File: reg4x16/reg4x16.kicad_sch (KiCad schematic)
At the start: 19 parts, among them J1 Conn_01x04, J2 Conn_01x01, U1 74LS670, U2 74LS670, U3 74LS670, U4 74LS670, U5 74AHC1G32, U6 74AHC1G32

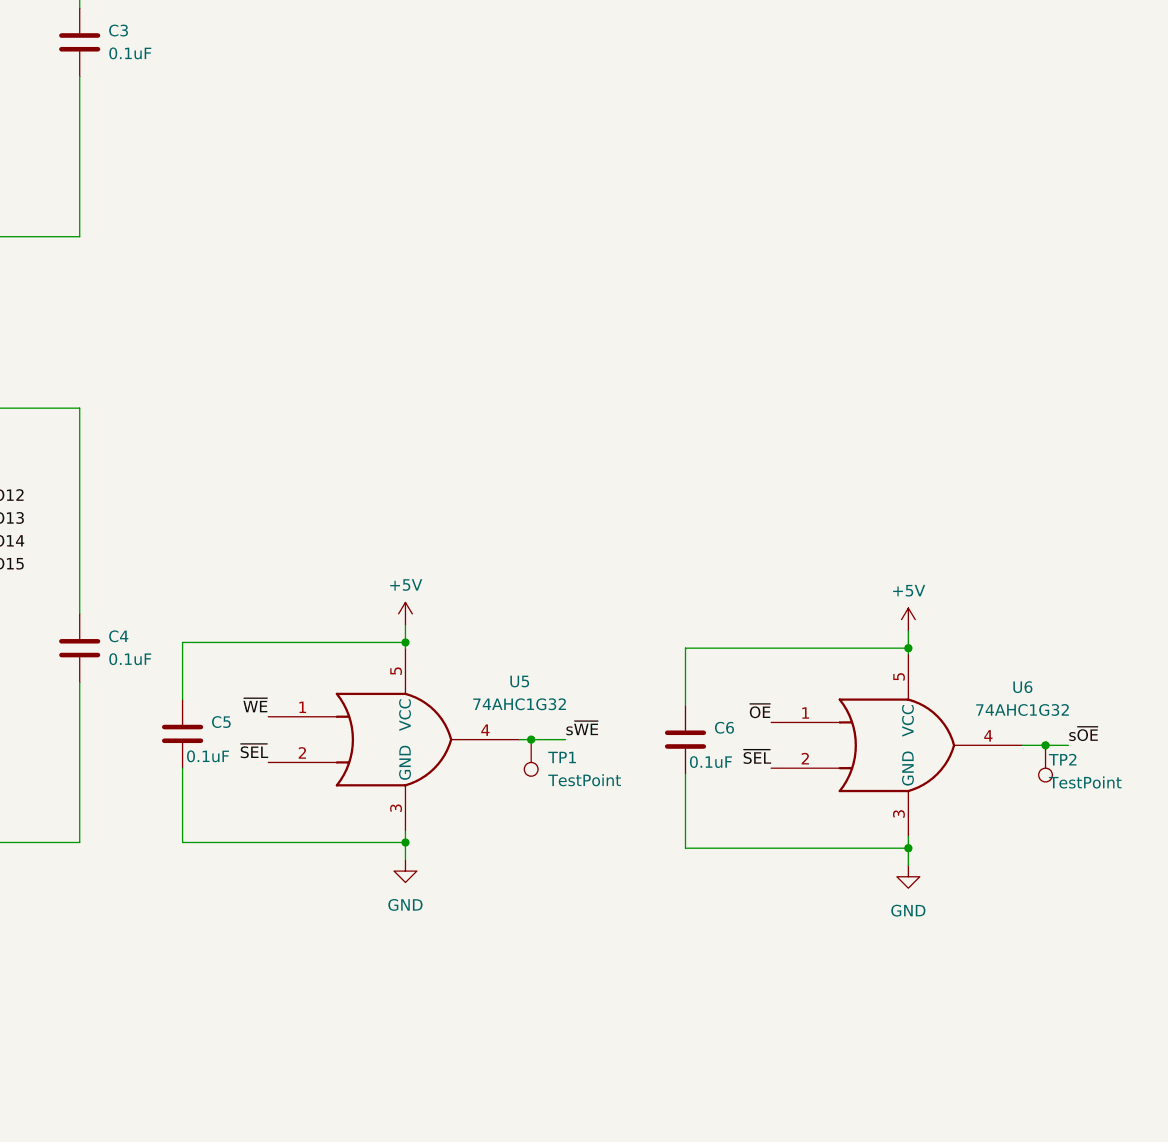
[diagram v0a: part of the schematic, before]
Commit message: Refactored files, finalized reg4x16, and used lowercase v
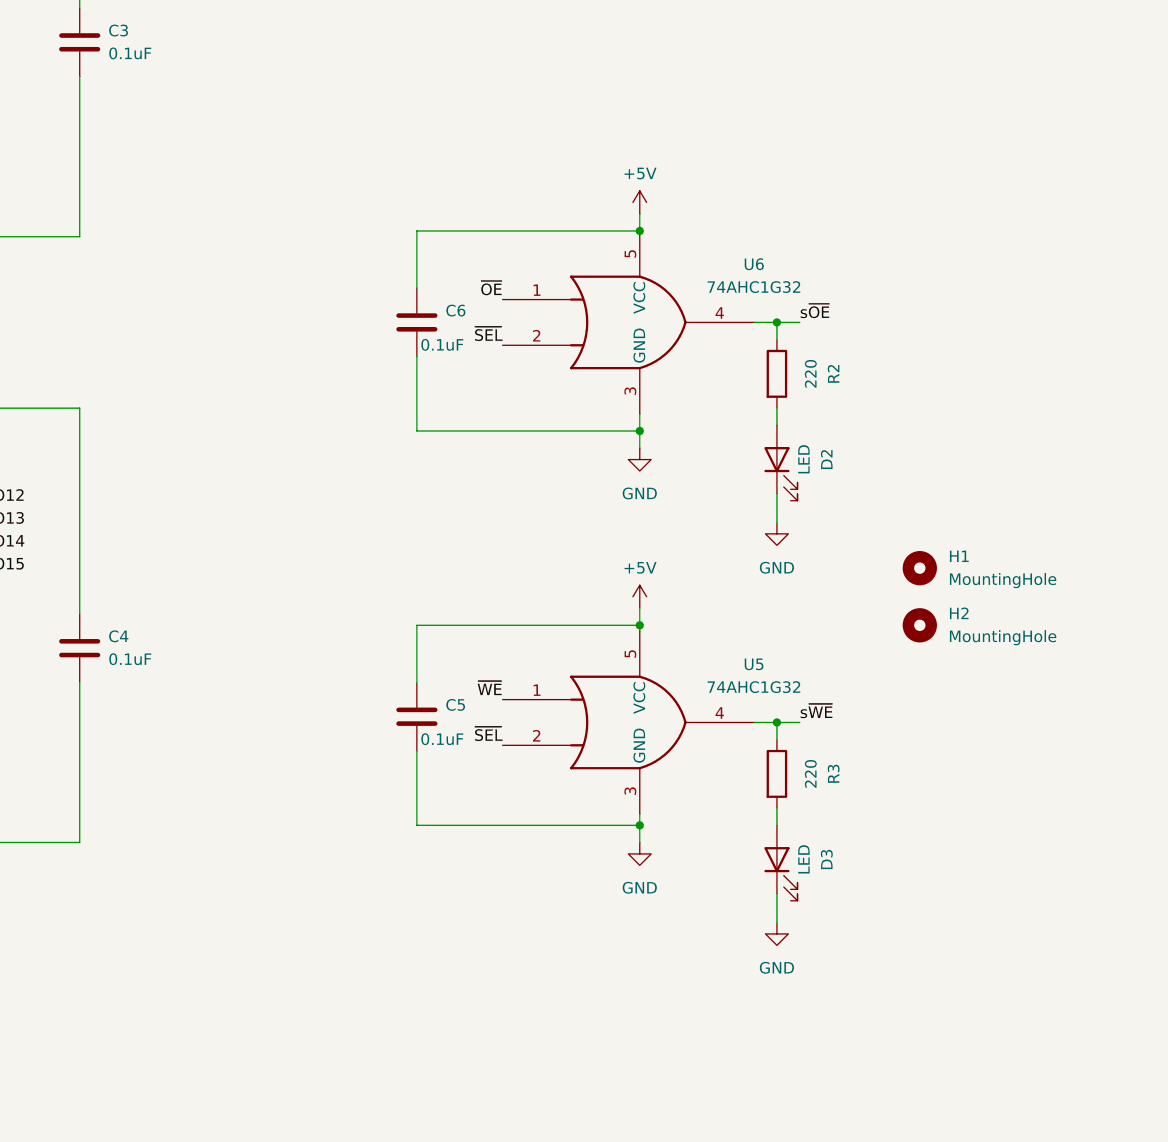
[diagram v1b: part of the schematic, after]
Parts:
- removed TP1, TP2: TestPoint, TestPoint:TestPoint_Pad_D2.0mm, symbol Connector:TestPoint
- added D2, D3: LED, LED_SMD:LED_0603_1608Metric, symbol Device:LED
- added H1, H2: MountingHole, MountingHole:MountingHole_2.2mm_M2, symbol Mechanical:MountingHole
- added R2, R3: 220, Resistor_SMD:R_0603_1608Metric, symbol Device:R
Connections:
- net GND: now also D2.1 (K), D3.1 (K)
- net s~{OE}: now also R2.1
- net s~{WE}: now also R3.1
- new net: D3.2 (A), R3.2
- new net: D2.2 (A), R2.2
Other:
- moved on the sheet: C5, C6, U5, U6
